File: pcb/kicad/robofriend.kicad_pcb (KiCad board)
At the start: 2 copper layers, 51 parts, among them J1 I2C, J10 VBAT, J11 Pwr_Terminal, J12 BOOST1, J13 Conn_02x05, J14 Conn_02x05, J15 UART, J16 AUDIOAMP, J2 ADC1, J3 ADC2, J4 UART, J5 ADC3, J6 ADC4, J7 BOOST2, J8 MONITOR, J9 Pwr_Terminal, K1 SANYOU_SRD_Form_A, U1 Teensy++2.0, U2 LM4040

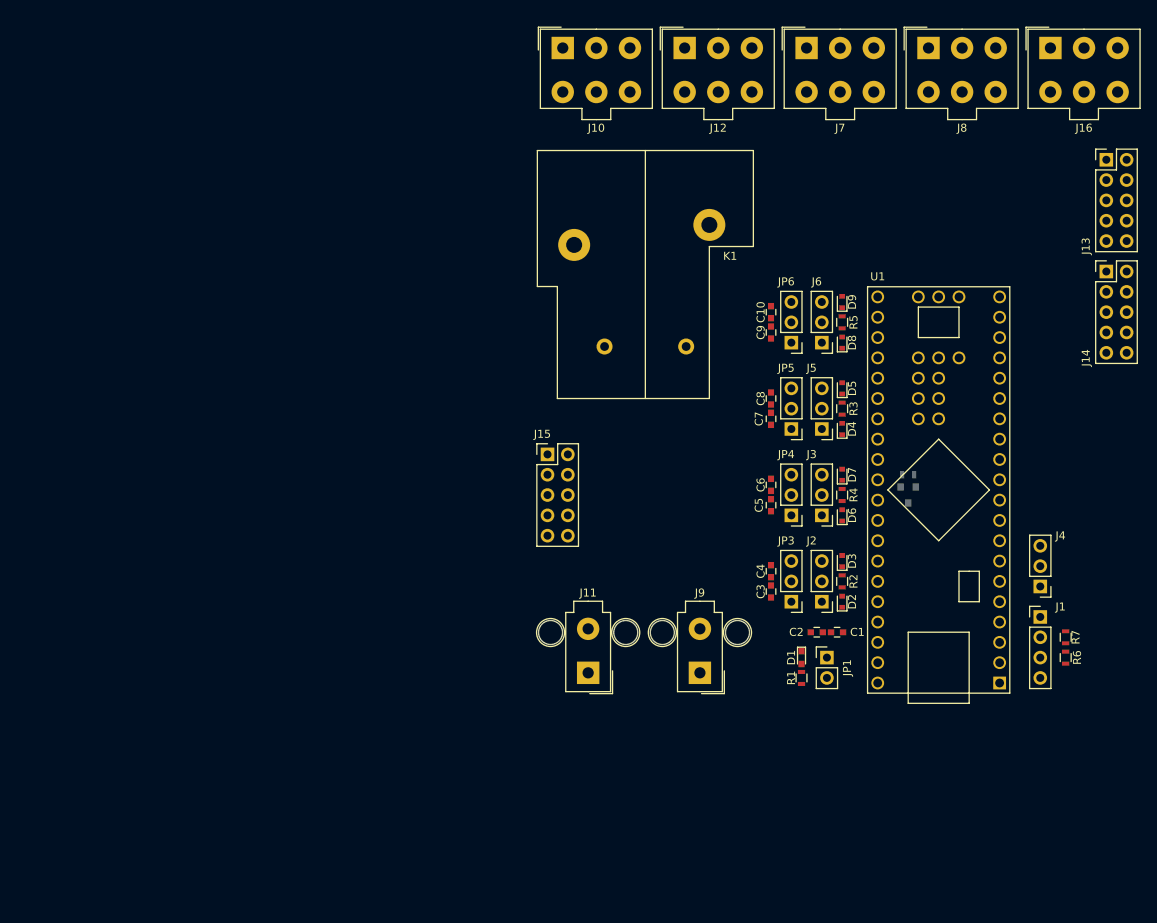
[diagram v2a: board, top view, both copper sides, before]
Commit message: adding interfaces for sensors, changing relay footprint, adapting power plugs, adapting further circuits, adapting parts and packages
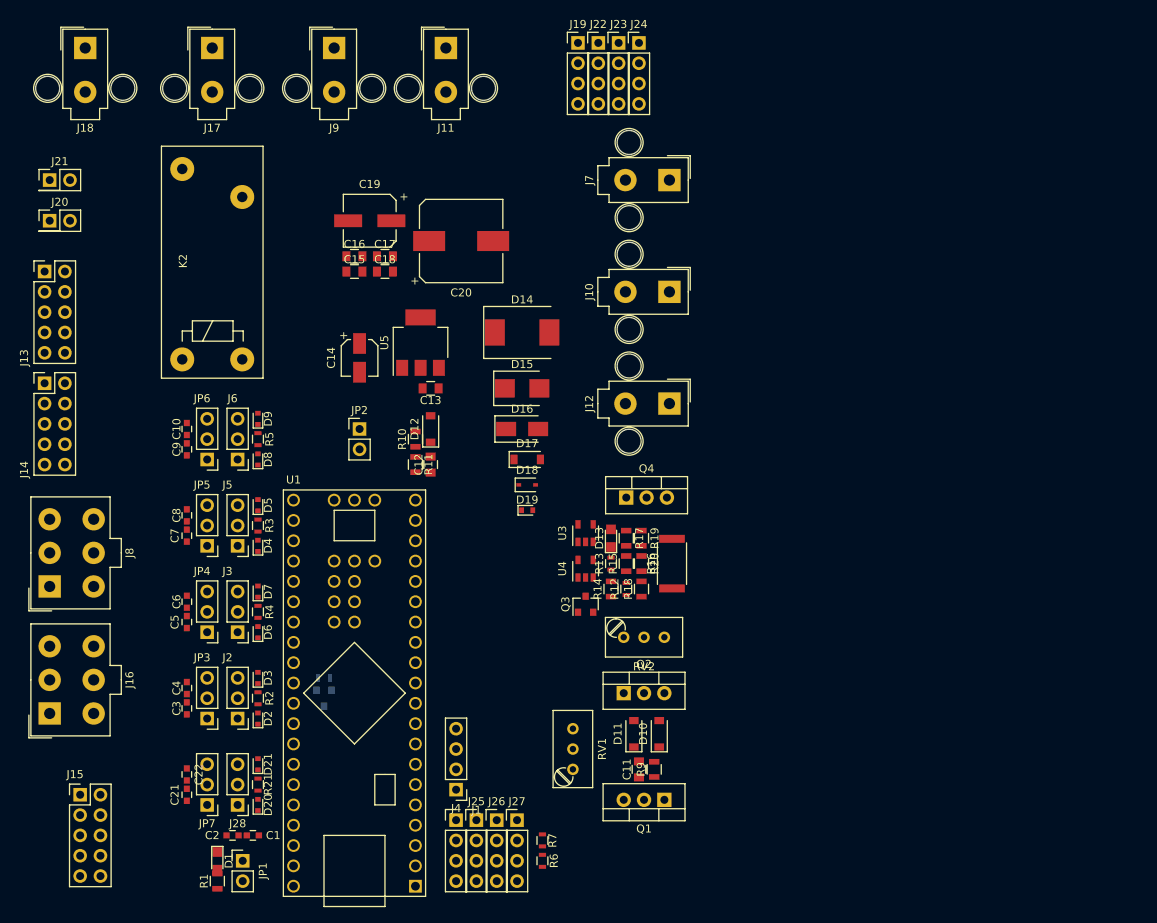
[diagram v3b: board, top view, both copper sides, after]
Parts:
- removed K1: SANYOU_SRD_Form_A, SLA_12VDC:SLA-12VDC
- added C11: 15n, Capacitors_SMD:C_0805, F.Cu at (90.8, 172.1)
- added C12: 100n, Capacitors_SMD:C_0805, F.Cu at (64.8, 134.0)
- added C13: 470n, Capacitors_SMD:C_0805, F.Cu at (64.8, 124.5)
- added C14: 33u, Capacitors_SMD:CP_Elec_4x5.8, F.Cu at (55.9, 120.7)
- added C15: 100n, Capacitors_SMD:C_0805, F.Cu at (55.2, 109.9)
- added C16: 100n, Capacitors_SMD:C_0805, F.Cu at (55.2, 108.0)
- added C17: 4,7u, Capacitors_SMD:C_0805, F.Cu at (59.1, 108.0)
- added C18: 4,7u, Capacitors_SMD:C_0805, F.Cu at (59.1, 109.9)
- added C19: 47u, Capacitors_SMD:CP_Elec_6.3x5.3, F.Cu at (57.1, 103.5)
- added C20: 470u, Capacitors_SMD:CP_Elec_10x10, F.Cu at (68.6, 106.0)
- added C21: 100n, Capacitors_SMD:C_0603, F.Cu at (34.3, 175.3)
- added C22: 100n, Capacitors_SMD:C_0603, F.Cu at (34.3, 172.7)
- added D10: 10V, Diodes_SMD:D_SOD-123, F.Cu at (93.3, 167.6)
- added D11: D, Diodes_SMD:D_SOD-123, F.Cu at (90.2, 167.6)
- added D12: 5V1, Diodes_SMD:D_SOD-123, F.Cu at (64.8, 129.5)
- added D13: LED, LEDs:LED_0805, F.Cu at (87.3, 143.2)
- added D14: D, Diodes_SMD:D_SMC, F.Cu at (76.2, 117.5)
- added D15: D, Diodes_SMD:D_SMB, F.Cu at (76.2, 124.5)
- added D16: D, Diodes_SMD:D_SMA, F.Cu at (76.2, 129.5)
- added D17: D, Diodes_SMD:D_SOD-123, F.Cu at (76.8, 133.3)
- added D18: D, Diodes_SMD:D_SOD-323, F.Cu at (76.8, 136.5)
- added D19: D, Diodes_SMD:D_SOD-523, F.Cu at (76.8, 139.7)
- added D20: D, Diodes_SMD:D_SOD-523, F.Cu at (43.2, 176.5)
- added D21: D, Diodes_SMD:D_SOD-523, F.Cu at (43.2, 171.4)
- added J17: M1, Connectors_Molex:Molex_MiniFit-JR-5556-02B_2x01x4.20mm_Straight, F.Cu at (37.5, 81.9)
- added J18: M2, Connectors_Molex:Molex_MiniFit-JR-5556-02B_2x01x4.20mm_Straight, F.Cu at (21.6, 81.9)
- added J19: Conn_01x04, Pin_Headers:Pin_Header_Straight_1x04_Pitch2.54mm, F.Cu at (83.2, 81.3)
- added J20: 5VOUT, Pin_Headers:Pin_Header_Straight_2x01_Pitch2.54mm, F.Cu at (17.1, 103.5)
- added J21: 5VOUT, Pin_Headers:Pin_Header_Straight_2x01_Pitch2.54mm, F.Cu at (17.1, 98.4)
- added J22: Conn_01x04, Pin_Headers:Pin_Header_Straight_1x04_Pitch2.54mm, F.Cu at (85.7, 81.3)
- added J23: Conn_01x04, Pin_Headers:Pin_Header_Straight_1x04_Pitch2.54mm, F.Cu at (88.3, 81.3)
- added J24: Conn_01x04, Pin_Headers:Pin_Header_Straight_1x04_Pitch2.54mm, F.Cu at (90.8, 81.3)
- added J25: I2C, Pin_Headers:Pin_Header_Straight_1x04_Pitch2.54mm, F.Cu at (70.5, 178.4)
- added J26: I2C, Pin_Headers:Pin_Header_Straight_1x04_Pitch2.54mm, F.Cu at (73.0, 178.4)
- added J27: I2C, Pin_Headers:Pin_Header_Straight_1x04_Pitch2.54mm, F.Cu at (75.6, 178.4)
- added J28: ADC4, Pin_Headers:Pin_Header_Straight_1x03_Pitch2.54mm, F.Cu at (40.6, 176.5)
- added JP2: JP, Pin_Headers:Pin_Header_Straight_1x02_Pitch2.54mm, F.Cu at (55.9, 129.5)
- added JP7: Jumper, Pin_Headers:Pin_Header_Straight_1x03_Pitch2.54mm, F.Cu at (36.8, 176.5)
- added K2: SCHRACK-RTx3, SLA_12VDC:Relay_SPST_Schrack-RTx3_RM3.5mm, F.Cu at (31.1, 123.2)
- added Q1: NMOS, TO_SOT_Packages_THT:TO-220-3_Vertical, F.Cu at (94.0, 175.9)
- added Q2: NMOS, TO_SOT_Packages_THT:TO-220-3_Vertical, F.Cu at (88.9, 162.6)
- added Q3: NPN, TO_SOT_Packages_SMD:SOT-23, F.Cu at (84.1, 151.4)
- added Q4: PMOS, TO_SOT_Packages_THT:TO-220-3_Vertical, F.Cu at (89.2, 138.1)
- added R10: 100k, Resistors_SMD:R_0805, F.Cu at (62.9, 130.8)
- added R11: 27k, Resistors_SMD:R_0805, F.Cu at (62.9, 134.0)
- added R12: 1k, Resistors_SMD:R_0603, F.Cu at (89.2, 149.5)
- added R13: 10k, Resistors_SMD:R_0603, F.Cu at (87.3, 146.4)
- added R14: 1k, Resistors_SMD:R_0805, F.Cu at (87.3, 149.5)
- added R15: 1k, Resistors_SMD:R_0805, F.Cu at (89.2, 146.4)
- added R16: 0.01, Resistors_SMD:R_2512, F.Cu at (94.9, 146.4)
- added R17: 1k, Resistors_SMD:R_0805, F.Cu at (89.2, 143.2)
- added R18: 1k, Resistors_SMD:R_0805, F.Cu at (91.1, 149.5)
- added R19: 33k, Resistors_SMD:R_0805, F.Cu at (91.1, 143.2)
- added R20: 33k, Resistors_SMD:R_0805, F.Cu at (91.1, 146.4)
- added R21: 100k, Resistors_SMD:R_0603, F.Cu at (43.2, 174.0)
- added R9: 12k, Resistors_SMD:R_0805, F.Cu at (92.7, 172.1)
- added RV1: POT_TRIM, Potentiometers:Potentiometer_Trimmer_Bourns_3296W, F.Cu at (82.5, 172.1)
- added RV2: POT_TRIM, Potentiometers:Potentiometer_Trimmer_Bourns_3296W, F.Cu at (88.9, 155.6)
- added U3: LM321, TO_SOT_Packages_SMD:SOT-23-5, F.Cu at (84.1, 142.6)
- added U4: LM321, TO_SOT_Packages_SMD:SOT-23-5, F.Cu at (84.1, 147.0)
- added U5: LM3940-3.3, TO_SOT_Packages_SMD:SOT-223, F.Cu at (63.5, 118.7)
- D1: footprint LEDs:LED_0603 -> LEDs:LED_0805
- J10: value VBAT -> BAT2; footprint Connectors_Molex:Molex_MiniFit-JR-5556-06A_2x03x4.20mm_Straight -> Connectors_Molex:Molex_MiniFit-JR-5556-02B_2x01x4.20mm_Straight
- J11: value Pwr_Terminal -> 5VIN
- J12: value BOOST1 -> BAT3; footprint Connectors_Molex:Molex_MiniFit-JR-5556-06A_2x03x4.20mm_Straight -> Connectors_Molex:Molex_MiniFit-JR-5556-02B_2x01x4.20mm_Straight
- J15: value UART -> SPI
- J4: footprint Pin_Headers:Pin_Header_Straight_1x03_Pitch2.54mm -> Pin_Headers:Pin_Header_Straight_1x04_Pitch2.54mm
- J7: value BOOST2 -> BAT1; footprint Connectors_Molex:Molex_MiniFit-JR-5556-06A_2x03x4.20mm_Straight -> Connectors_Molex:Molex_MiniFit-JR-5556-02B_2x01x4.20mm_Straight
- J9: value Pwr_Terminal -> 12VOUT
- R1: value 150 -> 1k; footprint Resistors_SMD:R_0603 -> Resistors_SMD:R_0805
- moved J16 150.2 mm to (17.1, 165.1), turned to 90 degrees
- moved J13 133.4 mm to (16.5, 109.9)
- moved J14 133.4 mm to (16.5, 123.8)
- moved J8 128.8 mm to (17.1, 149.2), turned to 90 degrees
- moved J9 90.5 mm to (52.7, 81.9), turned to 0 degrees
- moved J11 80.1 mm to (66.7, 81.9), turned to 0 degrees
- moved C2 77.3 mm to (40.0, 180.3)
- moved D1 77.3 mm to (38.1, 183.5)
- moved J1 77.3 mm to (67.9, 178.4)
- moved J4 77.3 mm to (67.9, 174.6)
- moved JP1 77.3 mm to (41.3, 183.5)
- moved R1 77.3 mm to (38.1, 186.1)
- moved U1 77.3 mm to (55.2, 162.6)
- moved C1 77.3 mm to (42.5, 180.3)
- moved R8 77.3 mm to (51.4, 160.7)
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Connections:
- net /AREF renamed AREF
- net /B0 renamed B0
- net /B1 renamed B1
- net /B2 renamed B2
- net /B3 renamed B3
- net /D0 renamed D0
- net /D1 renamed D1
- D1 pad 1: GND -> Net-(D1-Pad1)
- D2 pad 2: /F0 -> F1
- D3 pad 1: /F0 -> F1
- D4 pad 2: /F2 -> F3
- D5 pad 1: /F2 -> F3
- D6 pad 2: /F1 -> F2
- D7 pad 1: /F1 -> F2
- D8 pad 2: /F3 -> F4
- D9 pad 1: /F3 -> F4
- J10 pad 2: Net-(J10-Pad2) -> GND
- J11 pad 1: Net-(J11-Pad1) -> +5V
- J11 pad 2: Net-(J11-Pad2) -> GND
- J12 pad 1: Net-(J12-Pad1) -> Net-(J10-Pad1)
- J12 pad 2: Net-(J12-Pad2) -> GND
- J15 pad 5: /~RST -> RST
- J4 pad 1: /D2 -> +5V
- J4 pad 2: /D3 -> D2
- J4 pad 3: GND -> D3
- J7 pad 1: Net-(J7-Pad1) -> Net-(J10-Pad1)
- J7 pad 2: Net-(J7-Pad2) -> GND
- J9 pad 1: Net-(J9-Pad1) -> +12L
- J9 pad 2: Net-(J9-Pad2) -> GND
- R1 pad 1: +5V -> +12L
- R2 pad 1: /F0 -> F1
- R3 pad 1: /F2 -> F3
- R4 pad 1: /F1 -> F2
- R5 pad 1: /F3 -> F4
- U1 pad 2: /B7 -> B7
- U1 pad 20: /C7 -> C7
- U1 pad 23: Net-(U1-Pad23) -> RST
- U1 pad 26: /F5 -> F5
- U1 pad 27: /F4 -> F4
- U1 pad 28: /F3 -> F3
- U1 pad 29: /F2 -> F2
- U1 pad 30: /F1 -> F1
- U1 pad 31: /F0 -> F0
- U1 pad 35: /E7 -> E7
- U1 pad 5: /D2 -> D2
- U1 pad 6: /D3 -> D3
- U1 pad 7: /D4 -> D4
- U1 pad 8: /D5 -> D5
- U1 pad 9: /D6 -> D6

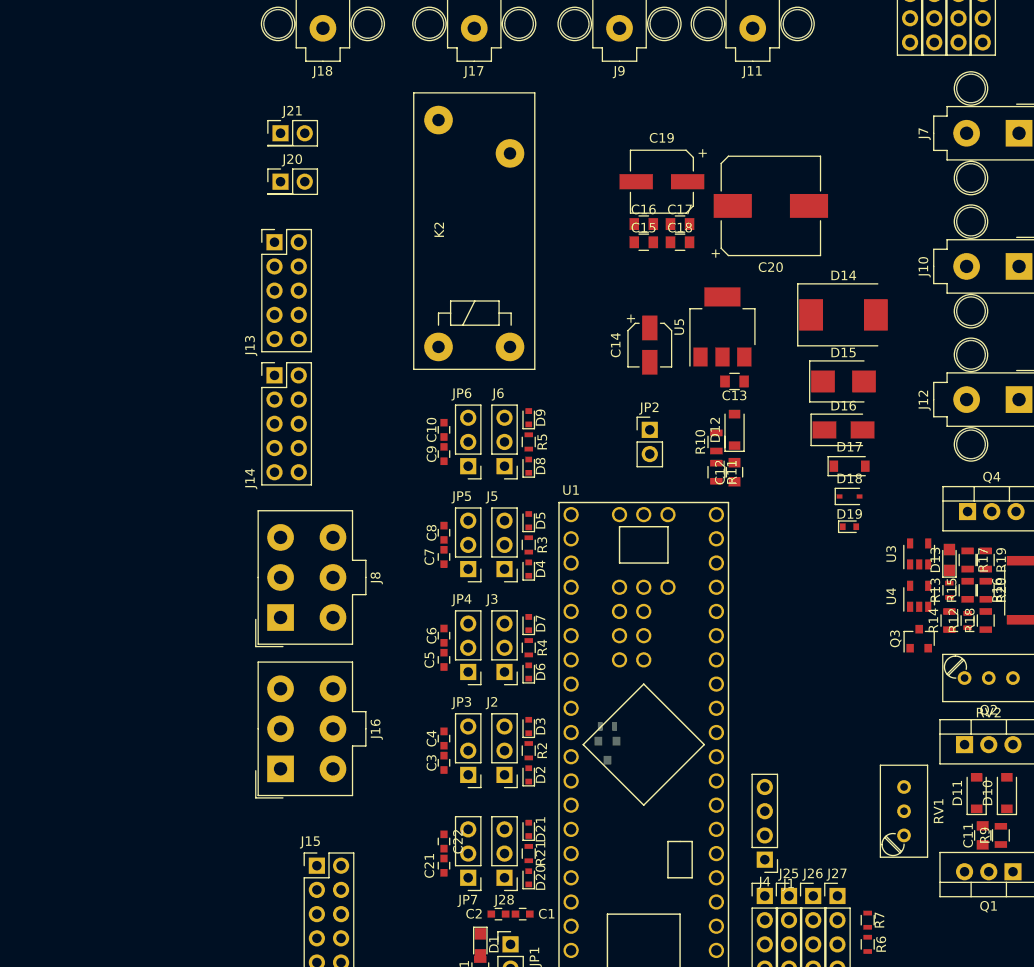
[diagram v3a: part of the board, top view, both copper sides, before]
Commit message: reviewing the schematic, missing the battery charge circuit still
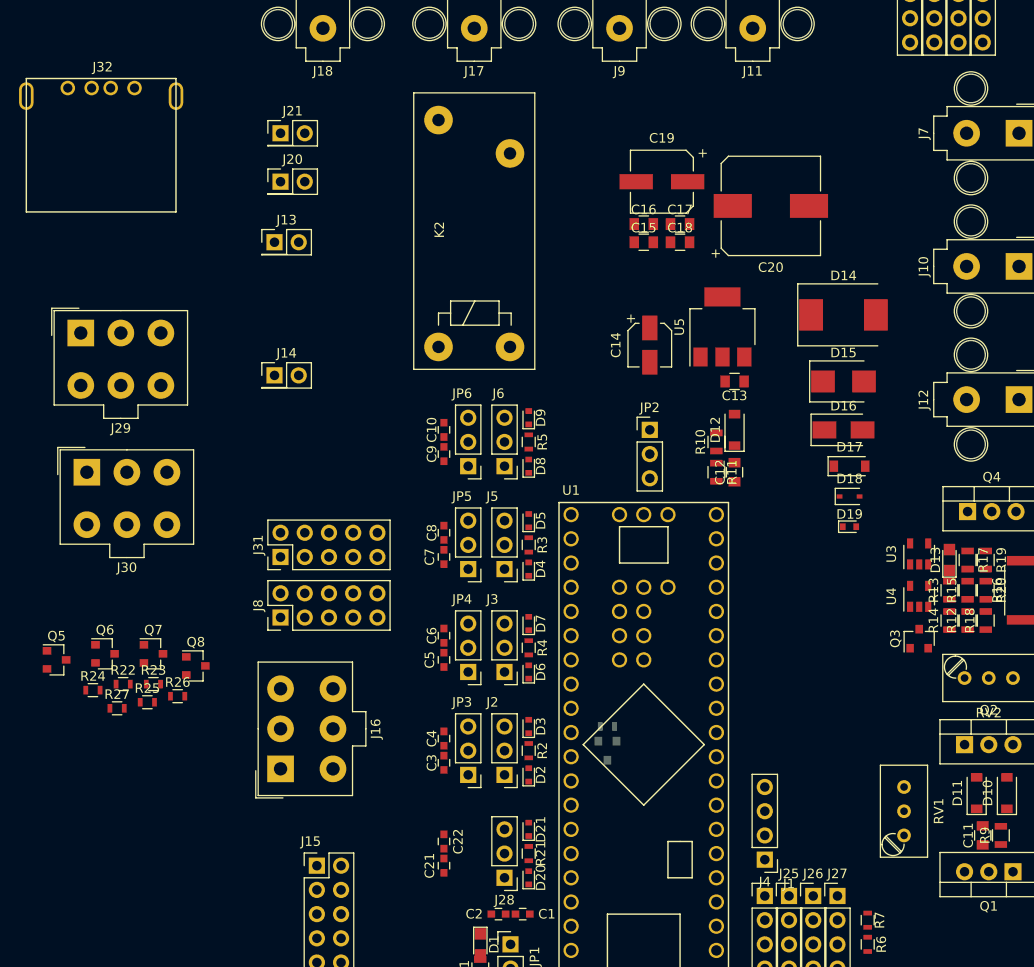
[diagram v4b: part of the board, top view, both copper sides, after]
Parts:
- removed JP7: Jumper, Pin_Headers:Pin_Header_Straight_1x03_Pitch2.54mm
- added J29: AMP, Connectors_Molex:Molex_MiniFit-JR-5556-06A_2x03x4.20mm_Straight, F.Cu at (-3.81, 119.4)
- added J30: PWR, Connectors_Molex:Molex_MiniFit-JR-5556-06A_2x03x4.20mm_Straight, F.Cu at (-3.17, 134.0)
- added J31: MLe, Pin_Headers:Pin_Header_Straight_2x05_Pitch2.54mm, F.Cu at (17.1, 142.9)
- added J32: USB_A_4_PIN, USB_A_4_PIN:MOLEX_48258_0001, F.Cu at (-9.53, 106.7)
- added Q5: NMOS, TO_SOT_Packages_SMD:SOT-23, F.Cu at (-6.35, 153.7)
- added Q6: NMOS, TO_SOT_Packages_SMD:SOT-23, F.Cu at (-1.27, 153.0)
- added Q7: NMOS, TO_SOT_Packages_SMD:SOT-23, F.Cu at (3.81, 153.0)
- added Q8: NMOS, TO_SOT_Packages_SMD:SOT-23, F.Cu at (8.26, 154.3)
- added R22: 10k, Resistors_SMD:R_0603, F.Cu at (0.64, 156.2)
- added R23: 10k, Resistors_SMD:R_0603, F.Cu at (3.81, 156.2)
- added R24: 10k, Resistors_SMD:R_0603, F.Cu at (-2.54, 156.8)
- added R25: 10k, Resistors_SMD:R_0603, F.Cu at (3.17, 158.1)
- added R26: 4.7k, Resistors_SMD:R_0603, F.Cu at (6.35, 157.5)
- added R27: 4.7k, Resistors_SMD:R_0603, F.Cu at (0.00, 158.8)
- J13, J14: value Conn_02x05 -> 3V3OUT; footprint Pin_Headers:Pin_Header_Straight_2x05_Pitch2.54mm -> Pin_Headers:Pin_Header_Straight_2x01_Pitch2.54mm
- J16: value AUDIOAMP -> MON
- J19: value Conn_01x04 -> US4
- J22: value Conn_01x04 -> US3
- J23: value Conn_01x04 -> US2
- J24: value Conn_01x04 -> US1
- J8: value MONITOR -> MRi; footprint Connectors_Molex:Molex_MiniFit-JR-5556-06A_2x03x4.20mm_Straight -> Pin_Headers:Pin_Header_Straight_2x05_Pitch2.54mm
- JP2: value JP -> Jumper; footprint Pin_Headers:Pin_Header_Straight_1x02_Pitch2.54mm -> Pin_Headers:Pin_Header_Straight_1x03_Pitch2.54mm
- R12, R13: footprint Resistors_SMD:R_0603 -> Resistors_SMD:R_0805
- R6, R7: value 1.8k -> 4.7k
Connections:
- C11 pad 2: +12L -> +SW
- C15 pad 2: +12L -> +SW
- C16 pad 2: +12L -> +SW
- C17 pad 2: +12L -> +SW
- C18 pad 2: +12L -> +SW
- C19 pad 1: +12L -> +SW
- C20 pad 1: +12L -> +SW
- D11 pad 1: +12L -> +SW
- D20 pad 1: Net-(D20-Pad1) -> +5V
- D8 pad 1: Net-(D8-Pad1) -> +5V
- J1 pad 1: +5V -> Net-(J1-Pad1)
- J1 pad 2: D1 -> Net-(J1-Pad2)
- J1 pad 3: D0 -> Net-(J1-Pad3)
- J10 pad 1: Net-(J10-Pad1) -> -SW
- J12 pad 1: Net-(J10-Pad1) -> -SW
- J13 pad 1: Net-(J13-Pad1) -> +3V3
- J13 pad 2: Net-(J13-Pad2) -> GND
- J14 pad 1: Net-(J14-Pad1) -> +3V3
- J14 pad 2: Net-(J14-Pad2) -> GND
- J19 pad 2: Net-(J19-Pad2) -> C6
- J19 pad 3: Net-(J19-Pad3) -> C7
- J22 pad 2: Net-(J22-Pad2) -> E1
- J22 pad 3: Net-(J22-Pad3) -> E0
- J23 pad 2: D6 -> D7
- J23 pad 3: C7 -> D6
- J25 pad 1: +5V -> Net-(J1-Pad1)
- J25 pad 2: D1 -> Net-(J1-Pad2)
- J25 pad 3: D0 -> Net-(J1-Pad3)
- J26 pad 1: +5V -> Net-(J1-Pad1)
- J26 pad 2: D1 -> Net-(J1-Pad2)
- J26 pad 3: D0 -> Net-(J1-Pad3)
- J27 pad 1: +5V -> Net-(J1-Pad1)
- J27 pad 2: D1 -> Net-(J1-Pad2)
- J27 pad 3: D0 -> Net-(J1-Pad3)
- J28 pad 1: Net-(D20-Pad1) -> +5V
- J4 pad 1: +5V -> Net-(J4-Pad1)
- J4 pad 2: D2 -> Net-(J4-Pad2)
- J4 pad 3: D3 -> Net-(J4-Pad3)
- J6 pad 1: Net-(D8-Pad1) -> +5V
- J7 pad 1: Net-(J10-Pad1) -> -SW
- J8 pad 1: Net-(J8-Pad1) -> GND
- J8 pad 2: Net-(J8-Pad2) -> B5
- J8 pad 3: Net-(J8-Pad3) -> B4
- J8 pad 4: Net-(J8-Pad4) -> C1
- J8 pad 5: Net-(J8-Pad5) -> C0
- J8 pad 6: Net-(J8-Pad6) -> +5V
- J9 pad 1: +12L -> +SW
- JP2 pad 1: Net-(J10-Pad1) -> +5V
- JP2 pad 2: +12L -> Net-(J4-Pad1)
- JP6 pad 2: Net-(D8-Pad1) -> Net-(J1-Pad1)
- K2 pad 11: Net-(J10-Pad1) -> -SW
- K2 pad 14: +12L -> +SW
- K2 pad A1: +12L -> +SW
- Q4 pad 3: +12L -> +SW
- R1 pad 1: +12L -> +SW
- R10 pad 2: +12L -> +SW
- R12 pad 2: B7 -> E7
- R14 pad 1: +12L -> +SW
- R6 pad 1: +5V -> Net-(J1-Pad1)
- R6 pad 2: D0 -> Net-(J1-Pad2)
- R7 pad 1: +5V -> Net-(J1-Pad1)
- R7 pad 2: D1 -> Net-(J1-Pad3)
- R9 pad 1: +12L -> +SW
- RV1 pad 1: +12L -> +SW
- U1 pad 10: /D7 -> D7
- U1 pad 11: /E0 -> E0
- U1 pad 12: /E1 -> E1
- U1 pad 13: /C0 -> C0
- U1 pad 14: /C1 -> C1
- U1 pad 15: /C2 -> C2
- U1 pad 16: /C3 -> C3
- U1 pad 17: /C4 -> C4
- U1 pad 18: /C5 -> C5
- U1 pad 19: /C6 -> C6
- U1 pad 21: Net-(U1-Pad21) -> Net-(C1-Pad1)
- U1 pad 22: Net-(U1-Pad22) -> GND
- U1 pad 34: /E6 -> E6
- U1 pad 40: /B4 -> B4
- U1 pad 41: /B5 -> B5
- U1 pad 42: /B6 -> B6
- U1 pad 43: Net-(C1-Pad1) -> Net-(U1-Pad43)
- U4 pad 4: E7 -> E6
